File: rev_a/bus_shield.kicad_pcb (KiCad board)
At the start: 2 copper layers, 100 x 50 mm, 42 parts, among them J1 TERMINATE_JUMPER, SW1 MJTP1243, U1 74HCT08, U2 LM2940, U3 MCP2562, U4 LM117T-3.3, U5 ATMEGA328_DIP28, X1 16MHz

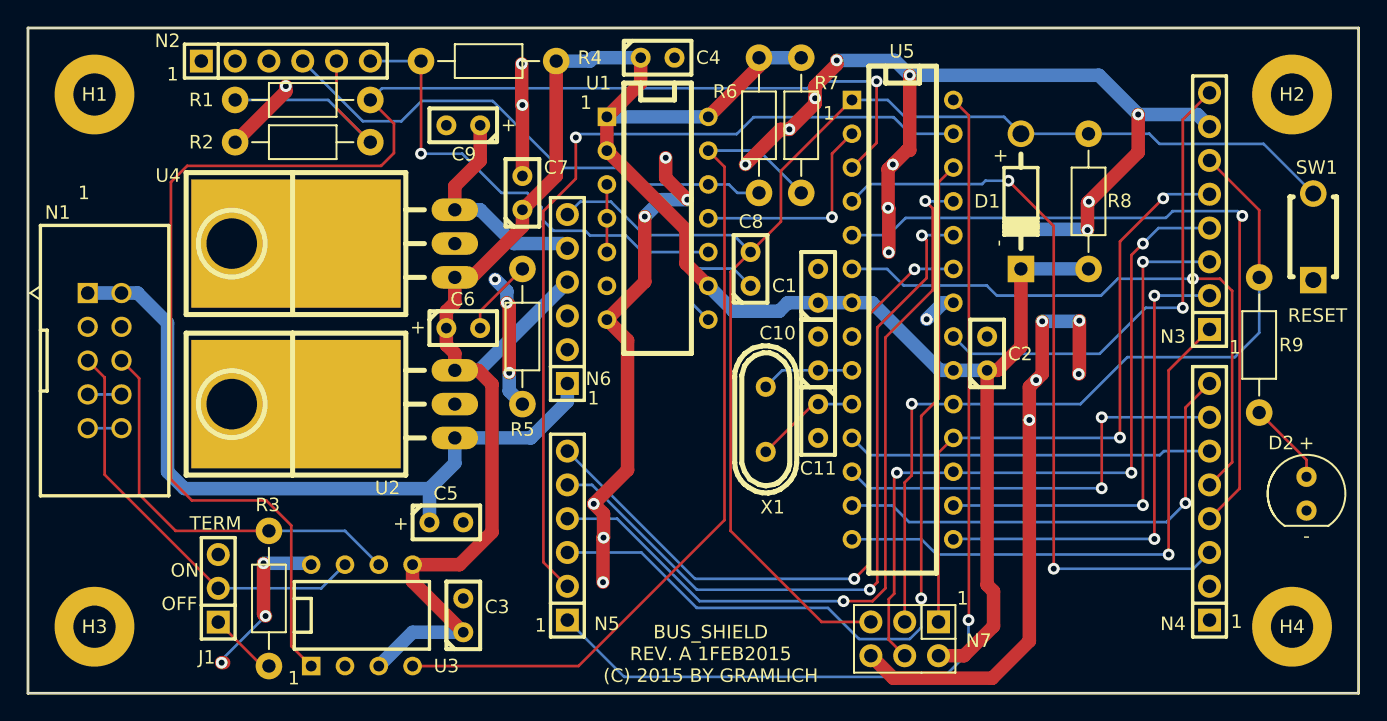
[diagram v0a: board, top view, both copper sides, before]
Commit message: Reset from bus circuit.
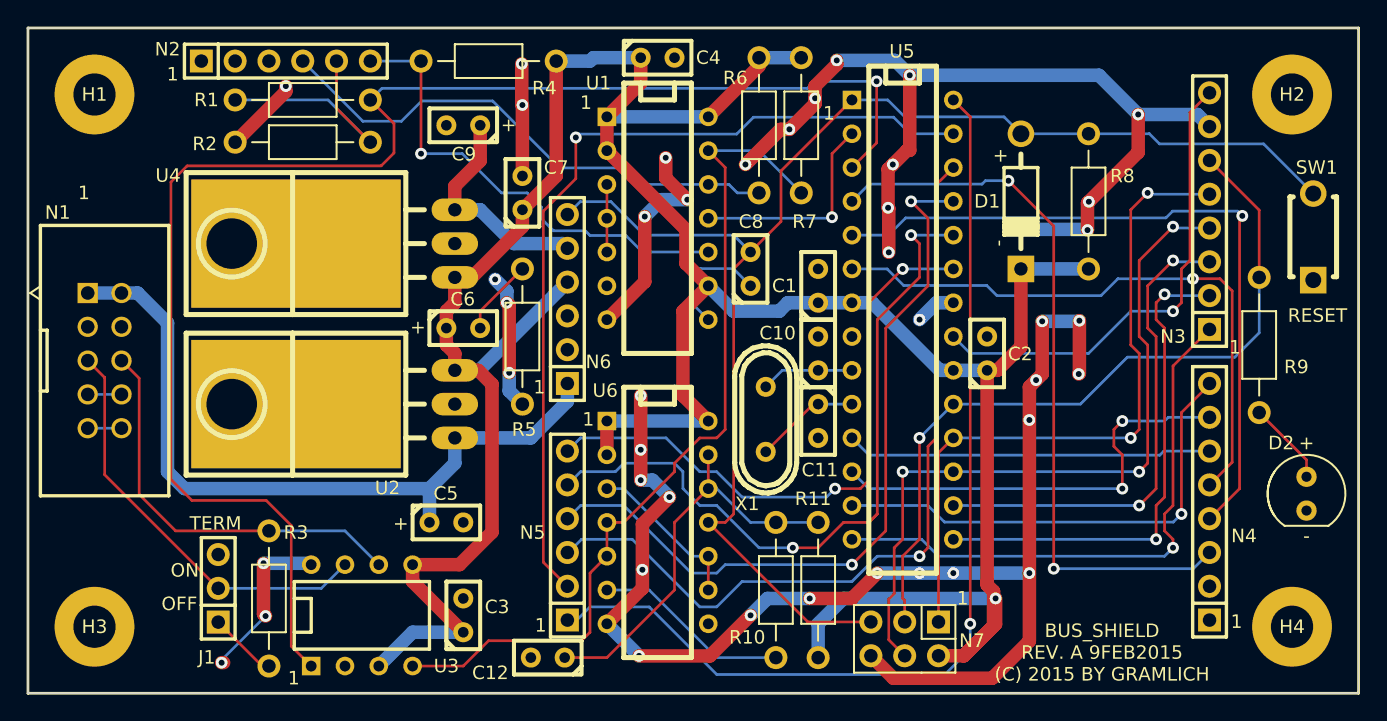
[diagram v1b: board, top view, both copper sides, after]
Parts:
- added C12: .1uF, bus_shield:Capacitor3MMDiscRM2.5, F.Cu at (139.1, 147.3)
- added R10: 180, bus_shield:Resistor_Horizontal_400, F.Cu at (156.2, 142.2)
- added R11: 10K, bus_shield:Resistor_Horizontal_400, F.Cu at (159.4, 142.2)
- added U6: 74HCT03, bus_shield:DIP-14__300, F.Cu at (147.3, 137.2)
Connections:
- net VCC renamed +5V
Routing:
- net +5V: track 181.7 -> 225.6 mm, vias 0 -> 1
- net GND: track 193.6 -> 228.2 mm, vias 33 -> 42
- net Net-(C12-Pad1): track 0.00 -> 30.9 mm
- net Net-(R10-Pad1): track 0.00 -> 14.8 mm
- net Net-(U6-Pad10): track 0.00 -> 12.9 mm
- net /A0: track 53.6 -> 46.2 mm
- net /A3: track 65.2 -> 60.8 mm
- net /~RESET: track 102.9 -> 105.6 mm
- net /A2: track 59.8 -> 57.5 mm
- net /D12: track 49.8 -> 51.8 mm
- net /A1: track 56.9 -> 55.0 mm
- net /D13: track 59.5 -> 57.7 mm
- net Net-(R7-Pad1): track 64.6 -> 65.7 mm
- net /D10: track 37.6 -> 36.8 mm
- net /A5: track 74.7 -> 75.4 mm
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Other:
- board text added: "BUS_SHIELD REV. A 9FEB2015 (C) 2015 BY GRAMLICH"
- board text removed: "BUS_SHIELD REV. A 1FEB2015 (C) 2015 BY GRAMLICH"
